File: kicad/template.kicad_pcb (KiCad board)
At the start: 2 copper layers, 84.1 x 61.7 mm, 8 parts, among them J1 Bus_PCI_Express_x1, J6 USB_C_Receptacle_USB2.0_16P, U2 RP2040, U4 W25Q128JVP, U9 MCP25625T-E/ML, X1 ABM8-272-T3

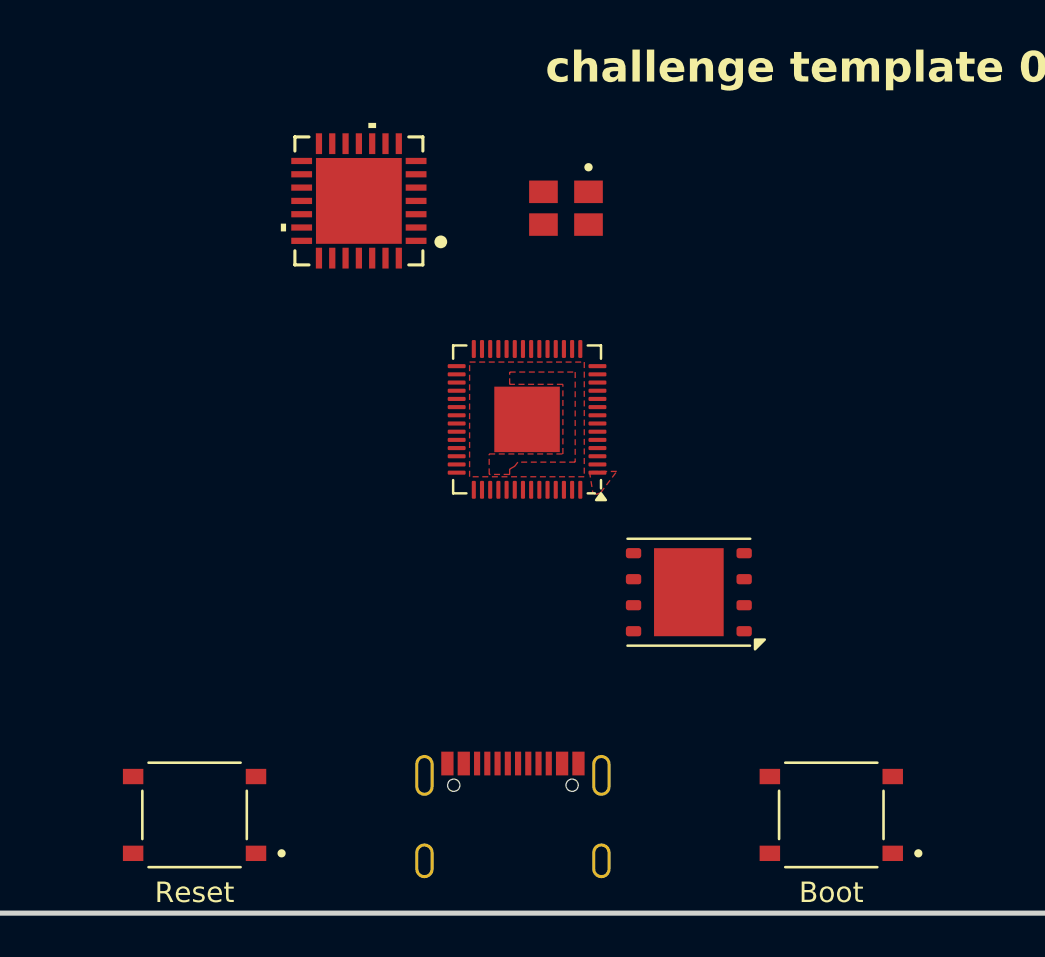
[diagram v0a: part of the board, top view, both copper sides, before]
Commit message: update to kicad 9, and delete everything from PCB editor
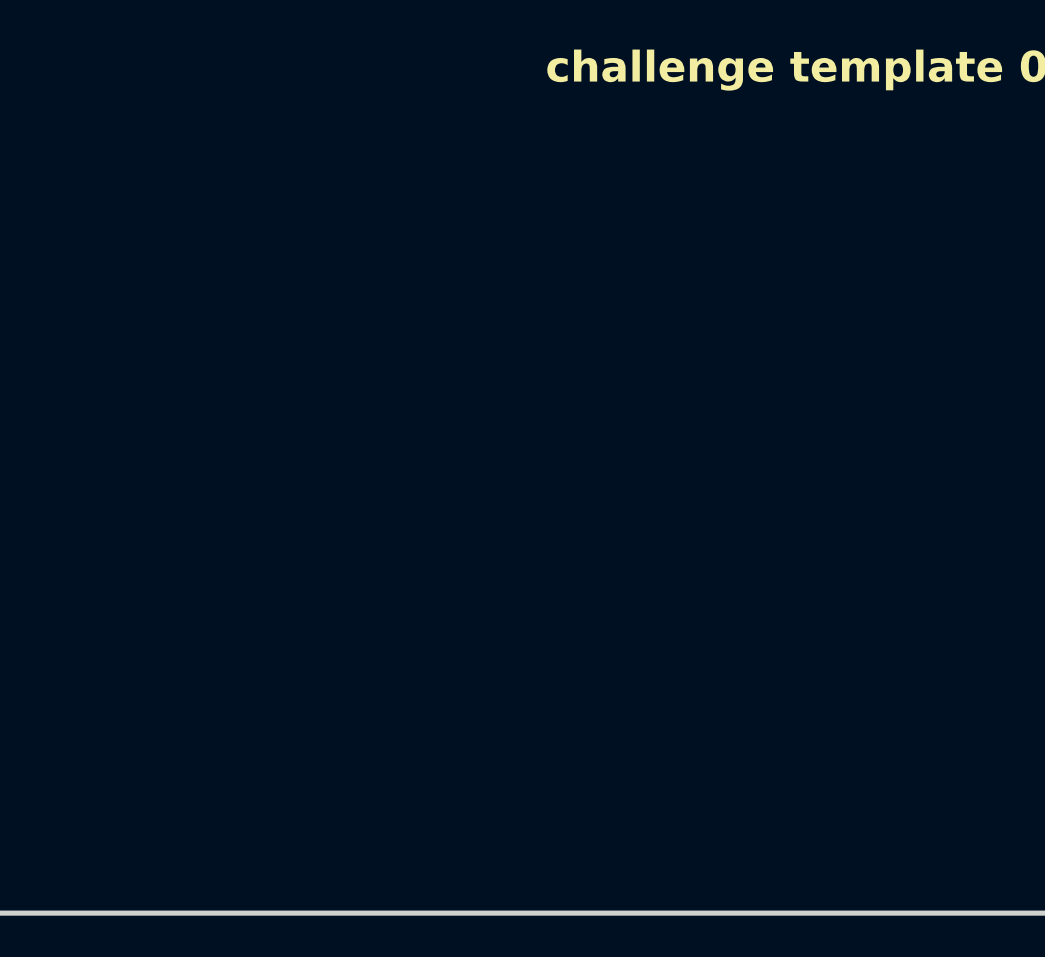
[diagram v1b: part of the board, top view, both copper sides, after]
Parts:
- removed J6: USB_C_Receptacle_USB2.0_16P, Connector_USB:USB_C_Receptacle_Palconn_UTC16-G
- removed S1, S2: TS-1187A-B-A-B, TS-1187A-B-A-B:SW_TS-1187A-B-A-B
- removed U2: RP2040, Package_DFN_QFN:QFN-56-1EP_7x7mm_P0.4mm_EP3.2x3.2mm
- removed U4: W25Q128JVP, Package_SON:WSON-8-1EP_6x5mm_P1.27mm_EP3.4x4.3mm
- removed U9: MCP25625T-E/ML, MCP25625T_E_ML:QFN28_6X6MC_MCH
- removed X1: ABM8-272-T3, ABM8-272-T3:ABM8-272-T3_ABR
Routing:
- removed copper zone on F.Cu, net +3.3V
- removed copper zone on F.Cu, net unconnected-(U2-VREG_VOUT-Pad45)
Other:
- board text removed: "Boot"
- board text removed: "Reset"
